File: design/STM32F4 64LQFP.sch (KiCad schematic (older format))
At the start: 15 parts, among them P7 SWD, U3 STM32F40X_LQFP64, X1 8MHz 10ppm

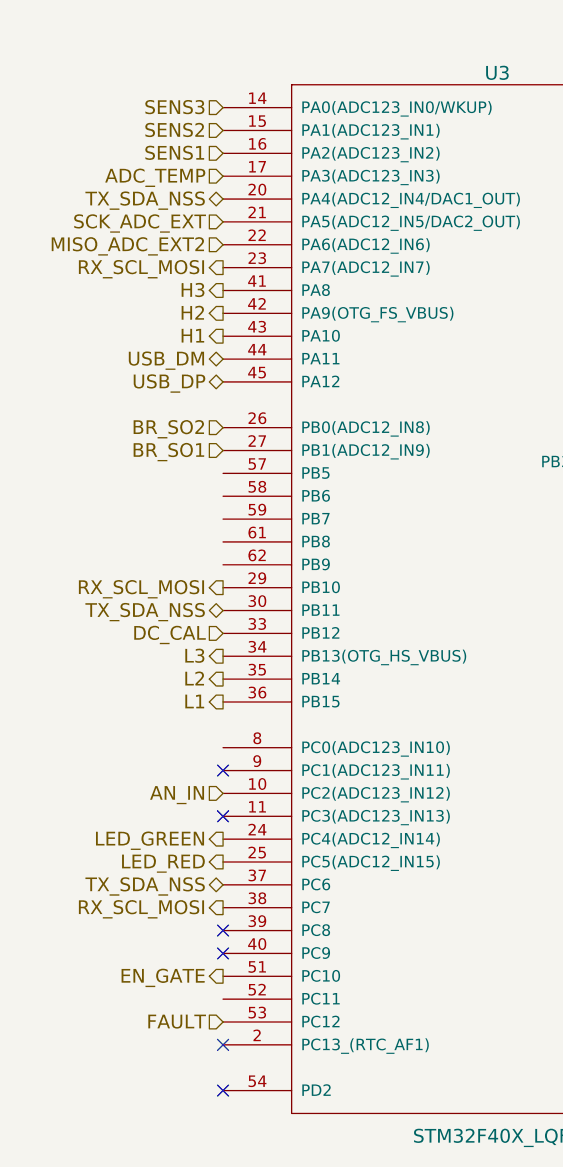
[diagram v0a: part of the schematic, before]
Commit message: Fixing ERC Errors :+1:
Turns out you need to mark pins as not connected. Who knew? Not me :sunglasses:
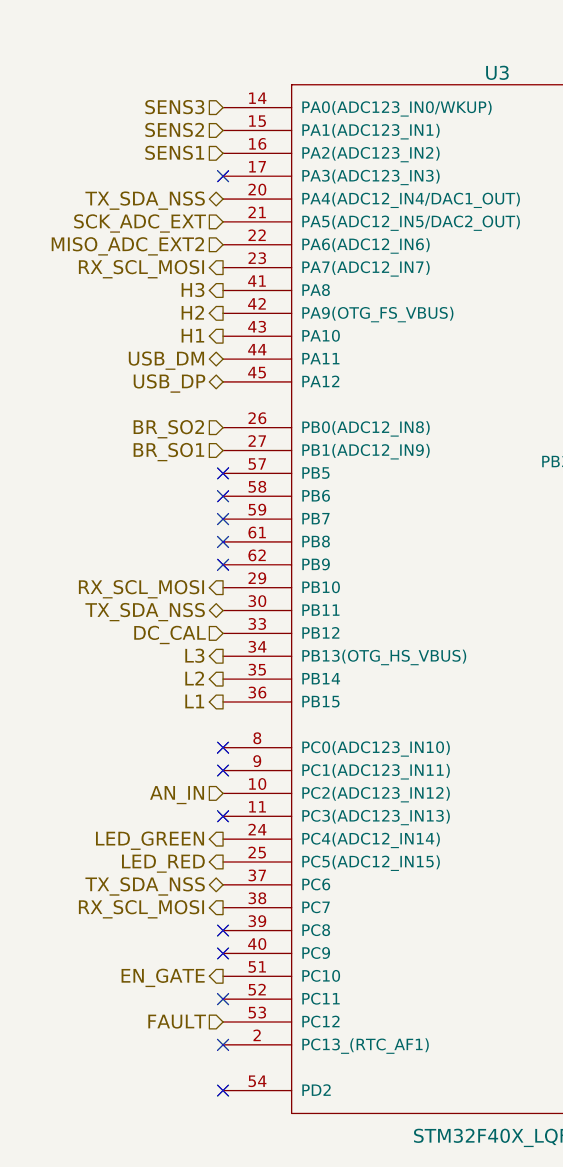
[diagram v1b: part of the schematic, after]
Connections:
- net ADC_TEMP: no longer names the net of U3.17 (PA3(ADC123_IN3))
- no-connect marks 13 -> 21
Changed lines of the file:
@@
 Text HLabel 4500 2450 0    60   Output ~ 0
 RX_SCL_MOSI
-Text HLabel 4500 2050 0    60   Input ~ 0
-ADC_TEMP
 Text HLabel 4500 2150 0    60   3State ~ 0
 TX_SDA_NSS
@@
 Wire Wire Line
 	10150 1000 10400 1000
+NoConn ~ 4500 3350
+NoConn ~ 4500 3450
+NoConn ~ 4500 3550
+NoConn ~ 4500 3650
+NoConn ~ 4500 3750
+NoConn ~ 4500 4550
+NoConn ~ 4500 5650
+NoConn ~ 4500 2050
 $EndSCHEMATC

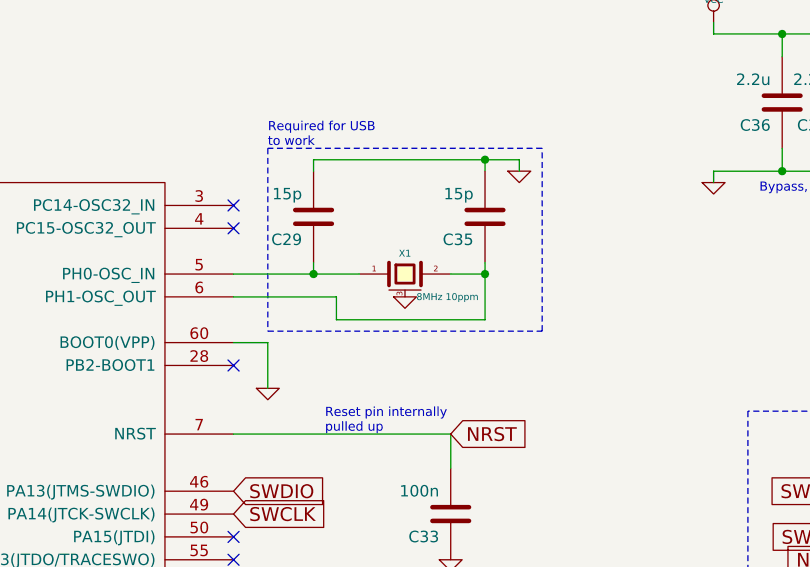
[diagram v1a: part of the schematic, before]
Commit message: Increasing current carrying capability
Added more vias and dedicated polygons to output stage.
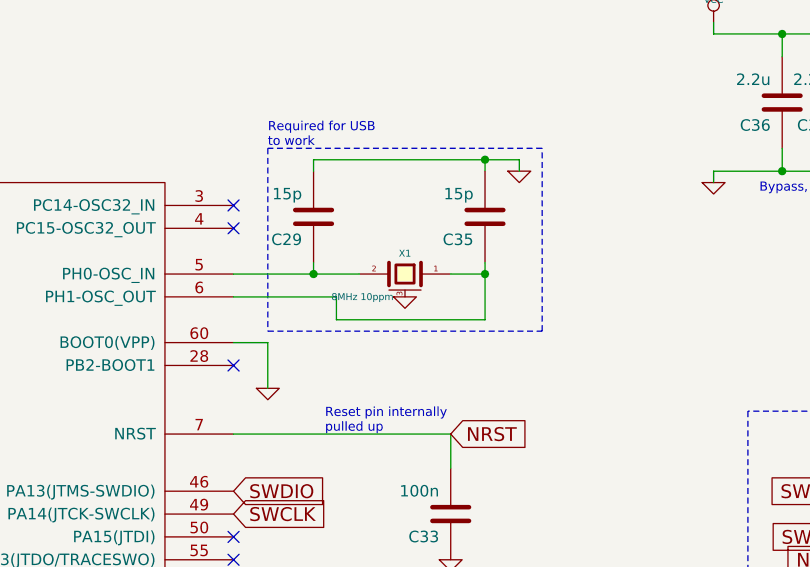
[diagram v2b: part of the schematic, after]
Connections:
- net at C29.1, U3.5 (PH0-OSC_IN): now also X1.2; no longer X1.1
- net at C35.1, U3.6 (PH1-OSC_OUT): now also X1.1; no longer X1.2
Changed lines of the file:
@@
 F 4 "ABM3B-8.0-10-1UT" H 7750 2050 60  0001 C CNN "mfg#"
 	1    7750 2050
-	1    0    0    -1
+	-1   0    0    -1
 $EndComp
 $Comp

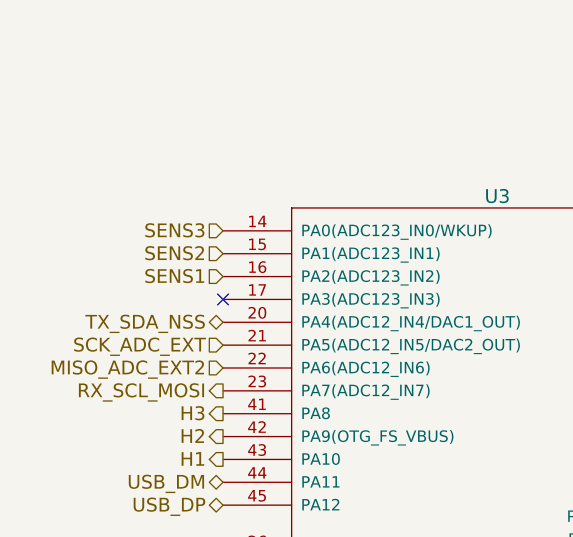
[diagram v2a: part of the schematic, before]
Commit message: Rework Board to fatten up supply
:snake: sneaky stuff :snake:
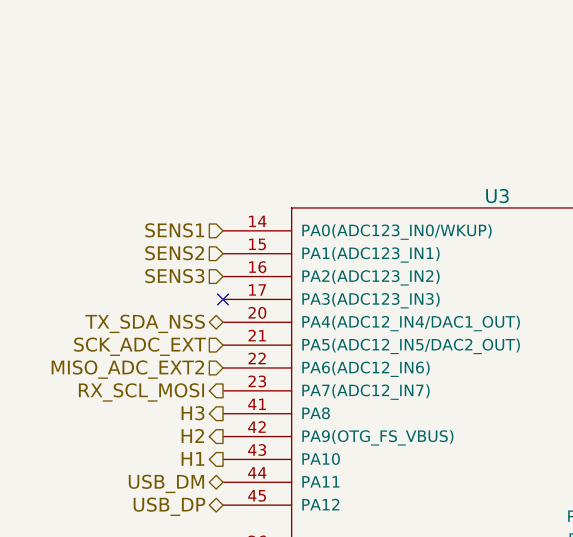
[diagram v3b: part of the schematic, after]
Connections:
- net SENS1: now also U3.14 (PA0(ADC123_IN0/WKUP)); no longer U3.16 (PA2(ADC123_IN2))
- net SENS3: now also U3.16 (PA2(ADC123_IN2)); no longer U3.14 (PA0(ADC123_IN0/WKUP))
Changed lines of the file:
@@
 Text HLabel 4500 2750 0    60   Output ~ 0
 H1
-Text HLabel 4500 1750 0    60   Input ~ 0
+Text HLabel 4500 1950 0    60   Input ~ 0
 SENS3
 Text HLabel 4500 1850 0    60   Input ~ 0
 SENS2
-Text HLabel 4500 1950 0    60   Input ~ 0
+Text HLabel 4500 1750 0    60   Input ~ 0
 SENS1
 Text HLabel 4500 3250 0    60   Input ~ 0

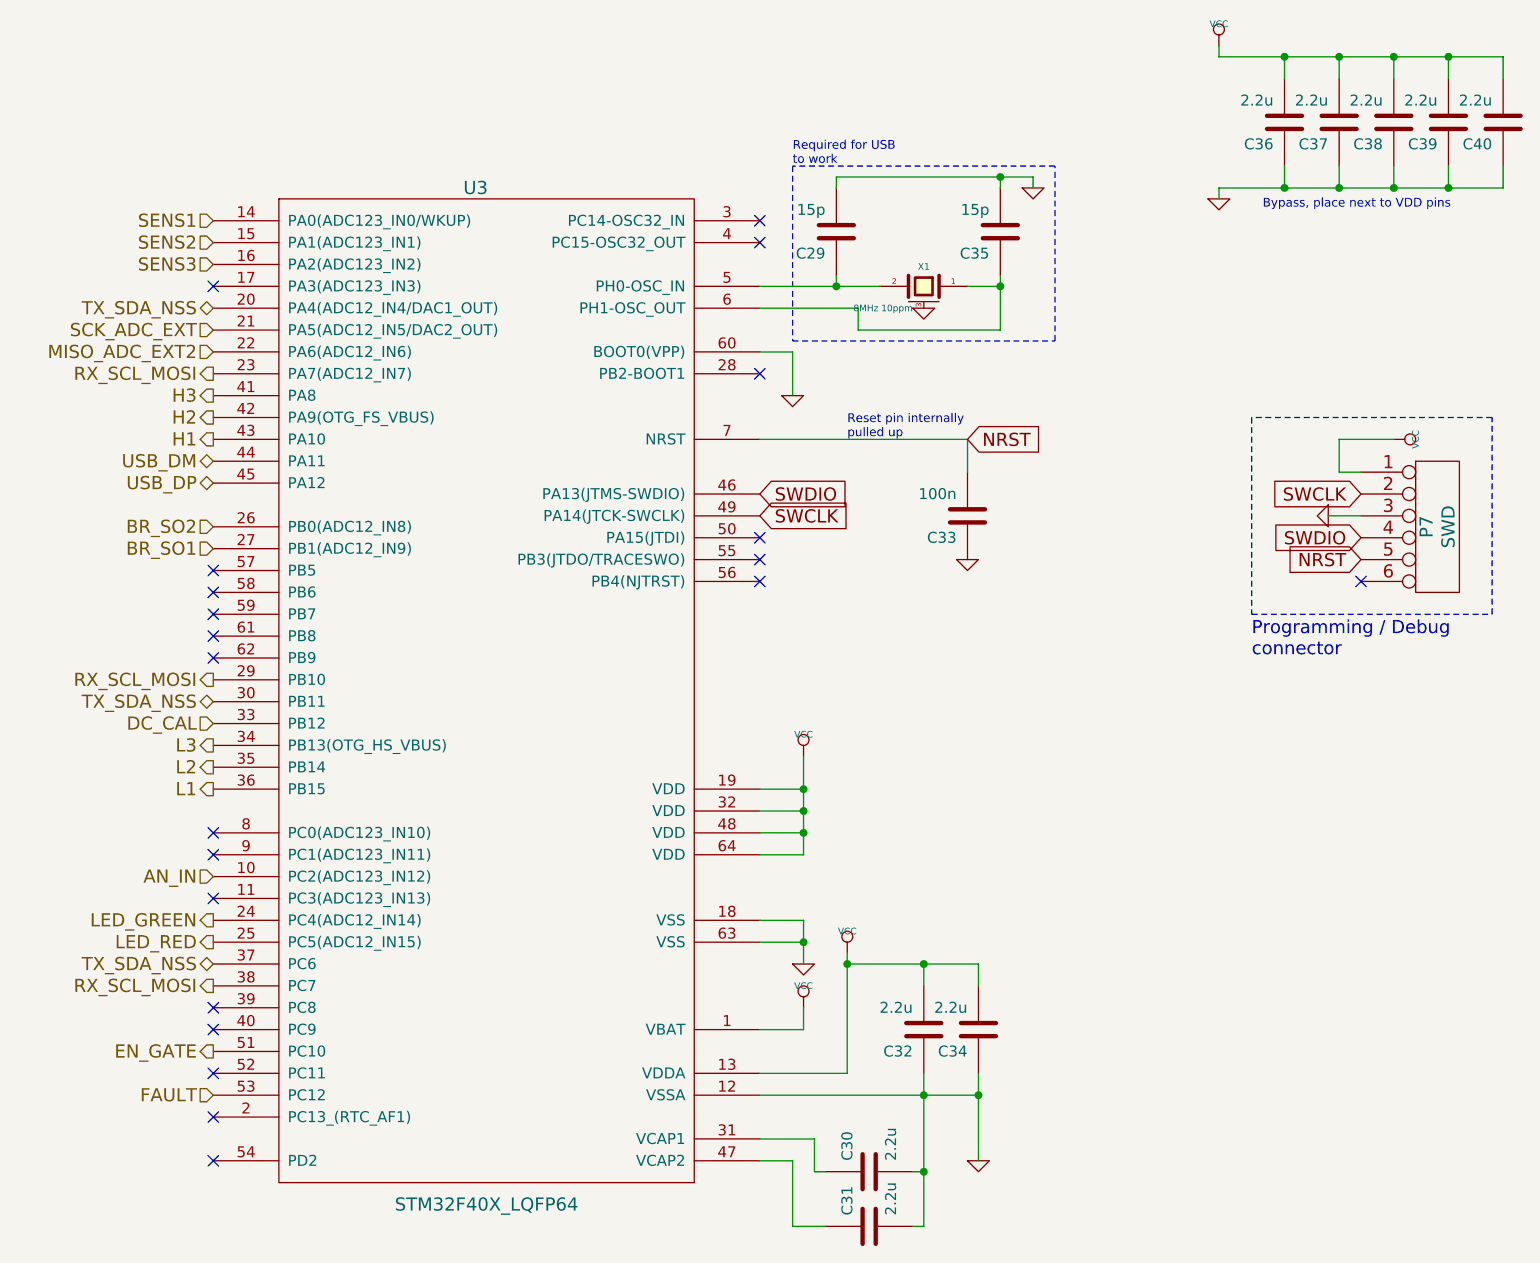
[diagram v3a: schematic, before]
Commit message: Added BOM and reworked component naming to be inline with old VESC names
:^)
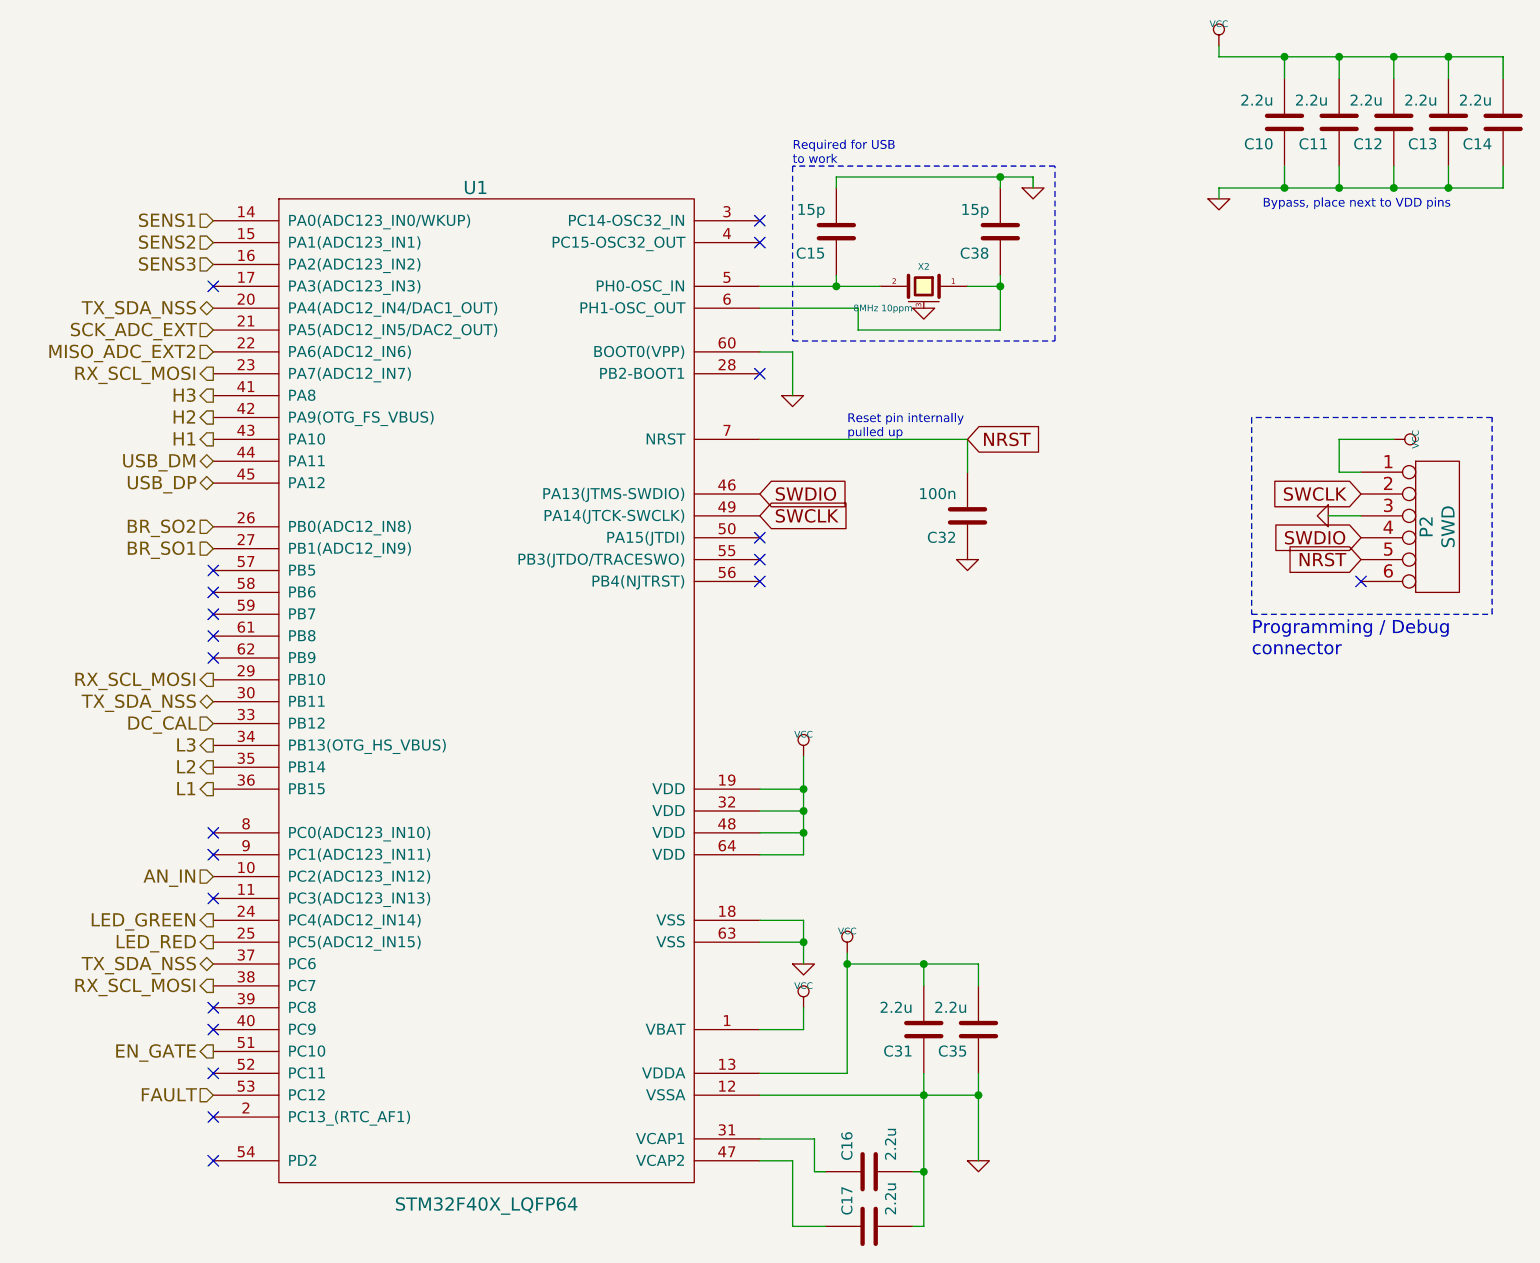
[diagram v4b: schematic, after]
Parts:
- renumbered C36 to C10, C37 to C11, C38 to C12, C39 to C13, C40 to C14, C29 to C15, C30 to C16, C31 to C17, C32 to C31, C33 to C32, C34 to C35, C35 to C38, P7 to P2, U3 to U1, X1 to X2
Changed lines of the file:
@@
 $EndDescr
 $Comp
-L crf_1:STM32F40X_LQFP64 U3
+L crf_1:STM32F40X_LQFP64 U1
 U 1 1 53F757A7
 P 5750 3900
-F 0 "U3" H 5700 6200 60  0000 C CNN
+F 0 "U1" H 5700 6200 60  0000 C CNN
 F 1 "STM32F40X_LQFP64" H 5750 1550 60  0000 C CNN
 F 2 "Package_QFP:LQFP-64_10x10mm_P0.5mm" H 5750 3900 60  0001 C CNN
@@
 P 7500 6350
 AR Path="/53F757AE" Ref="C?"  Part="1"
-AR Path="/53F7501A/53F757AE" Ref="C31"  Part="1"
-F 0 "C31" H 7550 6450 50  0000 L CNN
+AR Path="/53F7501A/53F757AE" Ref="C17"  Part="1"
+F 0 "C17" H 7550 6450 50  0000 L CNN
 F 1 "2.2u" H 7550 6250 50  0000 L CNN
 F 2 "Capacitor_SMD:C_0603_1608Metric" H 7500 6350 60  0001 C CNN
@@
 P 7500 6100
 AR Path="/53F757B5" Ref="C?"  Part="1"
-AR Path="/53F7501A/53F757B5" Ref="C30"  Part="1"
-F 0 "C30" H 7550 6200 50  0000 L CNN
+AR Path="/53F7501A/53F757B5" Ref="C16"  Part="1"
+F 0 "C16" H 7550 6200 50  0000 L CNN
 F 1 "2.2u" H 7550 6000 50  0000 L CNN
 F 2 "Capacitor_SMD:C_0603_1608Metric" H 7500 6100 60  0001 C CNN
@@
 P 7350 1800
 AR Path="/53F757DB" Ref="C?"  Part="1"
-AR Path="/53F7501A/53F757DB" Ref="C29"  Part="1"
-F 0 "C29" H 7400 1900 50  0000 L CNN
+AR Path="/53F7501A/53F757DB" Ref="C15"  Part="1"
+F 0 "C15" H 7400 1900 50  0000 L CNN
 F 1 "15p" H 7400 1700 50  0000 L CNN
 F 2 "Capacitor_SMD:C_0603_1608Metric" H 7350 1800 60  0001 C CNN
@@
 P 8100 1800
 AR Path="/53F757E2" Ref="C?"  Part="1"
-AR Path="/53F7501A/53F757E2" Ref="C35"  Part="1"
-F 0 "C35" H 8150 1900 50  0000 L CNN
+AR Path="/53F7501A/53F757E2" Ref="C38"  Part="1"
+F 0 "C38" H 8150 1900 50  0000 L CNN
 F 1 "15p" H 8150 1700 50  0000 L CNN
 F 2 "Capacitor_SMD:C_0603_1608Metric" H 8100 1800 60  0001 C CNN
@@
 P 7750 5450
 AR Path="/53F757F8" Ref="C?"  Part="1"
-AR Path="/53F7501A/53F757F8" Ref="C32"  Part="1"
-F 0 "C32" H 7800 5550 50  0000 L CNN
+AR Path="/53F7501A/53F757F8" Ref="C31"  Part="1"
+F 0 "C31" H 7800 5550 50  0000 L CNN
 F 1 "2.2u" H 7800 5350 50  0000 L CNN
 F 2 "Capacitor_SMD:C_0603_1608Metric" H 7750 5450 60  0001 C CNN
@@
 P 8000 5450
 AR Path="/53F757FF" Ref="C?"  Part="1"
-AR Path="/53F7501A/53F757FF" Ref="C34"  Part="1"
-F 0 "C34" H 8050 5550 50  0000 L CNN
+AR Path="/53F7501A/53F757FF" Ref="C35"  Part="1"
+F 0 "C35" H 8050 5550 50  0000 L CNN
 F 1 "2.2u" H 8050 5350 50  0000 L CNN
 F 2 "Capacitor_SMD:C_0603_1608Metric" H 8000 5450 60  0001 C CNN
@@
 P 7950 3100
 AR Path="/53F75896" Ref="C?"  Part="1"
-AR Path="/53F7501A/53F75896" Ref="C33"  Part="1"
-F 0 "C33" H 8000 3200 50  0000 L CNN
+AR Path="/53F7501A/53F75896" Ref="C32"  Part="1"
+F 0 "C32" H 8000 3200 50  0000 L CNN
 F 1 "100n" H 8000 3000 50  0000 L CNN
 F 2 "Capacitor_SMD:C_0603_1608Metric" H 7950 3100 60  0001 C CNN
@@
 NoConn ~ 4500 4850
 $Comp
-L BLDC_4-rescue:CONN_6 P7
+L BLDC_4-rescue:CONN_6 P2
 U 1 1 53F77410
 P 10100 3150
-F 0 "P7" V 10050 3150 60  0000 C CNN
+F 0 "P2" V 10050 3150 60  0000 C CNN
 F 1 "SWD" V 10150 3150 60  0000 C CNN
 F 2 "Connector_JST:JST_PH_B6B-PH-K_1x06_P2.00mm_Vertical" H 10100 3150 60  0001 C CNN
@@
 P 9400 1300
 AR Path="/53F77426" Ref="C?"  Part="1"
-AR Path="/53F7501A/53F77426" Ref="C36"  Part="1"
-F 0 "C36" H 9450 1400 50  0000 L CNN
+AR Path="/53F7501A/53F77426" Ref="C10"  Part="1"
+F 0 "C10" H 9450 1400 50  0000 L CNN
 F 1 "2.2u" H 9450 1200 50  0000 L CNN
 F 2 "Capacitor_SMD:C_0603_1608Metric" H 9400 1300 60  0001 C CNN
@@
 P 9650 1300
 AR Path="/53F7742D" Ref="C?"  Part="1"
-AR Path="/53F7501A/53F7742D" Ref="C37"  Part="1"
-F 0 "C37" H 9700 1400 50  0000 L CNN
+AR Path="/53F7501A/53F7742D" Ref="C11"  Part="1"
+F 0 "C11" H 9700 1400 50  0000 L CNN
 F 1 "2.2u" H 9700 1200 50  0000 L CNN
 F 2 "Capacitor_SMD:C_0603_1608Metric" H 9650 1300 60  0001 C CNN
@@
 P 10400 1300
 AR Path="/53F77434" Ref="C?"  Part="1"
-AR Path="/53F7501A/53F77434" Ref="C40"  Part="1"
-F 0 "C40" H 10450 1400 50  0000 L CNN
+AR Path="/53F7501A/53F77434" Ref="C14"  Part="1"
+F 0 "C14" H 10450 1400 50  0000 L CNN
 F 1 "2.2u" H 10450 1200 50  0000 L CNN
 F 2 "Capacitor_SMD:C_0603_1608Metric" H 10400 1300 60  0001 C CNN
@@
 P 9900 1300
 AR Path="/53F77447" Ref="C?"  Part="1"
-AR Path="/53F7501A/53F77447" Ref="C38"  Part="1"
-F 0 "C38" H 9950 1400 50  0000 L CNN
+AR Path="/53F7501A/53F77447" Ref="C12"  Part="1"
+F 0 "C12" H 9950 1400 50  0000 L CNN
 F 1 "2.2u" H 9950 1200 50  0000 L CNN
 F 2 "Capacitor_SMD:C_0603_1608Metric" H 9900 1300 60  0001 C CNN
@@
 P 10150 1300
 AR Path="/53F7744E" Ref="C?"  Part="1"
-AR Path="/53F7501A/53F7744E" Ref="C39"  Part="1"
-F 0 "C39" H 10200 1400 50  0000 L CNN
+AR Path="/53F7501A/53F7744E" Ref="C13"  Part="1"
+F 0 "C13" H 10200 1400 50  0000 L CNN
 F 1 "2.2u" H 10200 1200 50  0000 L CNN
 F 2 "Capacitor_SMD:C_0603_1608Metric" H 10150 1300 60  0001 C CNN
@@
 LED_GREEN
 $Comp
-L BLDC_4-rescue:CRYSTAL_SMD X1
+L BLDC_4-rescue:CRYSTAL_SMD X2
 U 1 1 540978A3
 P 7750 2050
-F 0 "X1" H 7750 2140 30  0000 C CNN
+F 0 "X2" H 7750 2140 30  0000 C CNN
 F 1 "8MHz 10ppm" H 7800 1950 30  0000 L CNN
 F 2 "Crystal:Crystal_SMD_5032-4Pin_5.0x3.2mm" H 7750 2050 60  0001 C CNN
